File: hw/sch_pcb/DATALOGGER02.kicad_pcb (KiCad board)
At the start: 4 copper layers, 101.1 x 60.5 mm, 161 parts, among them IC1 CY15B108QN-40SXI, IC2 FM3164-G, IC3 LTC4041EUFD#PBF, J1 HEADER_2x01_PARALLEL, J10 HEADER_2x05_PARALLEL, J11 HEADER_2x07_PARALLEL, J12 HEADER_2x05_PARALLEL, J13 HEADER_2x02_PARALLEL, J14 Conn_01x06_Female, J2 HEADER_2x01, J23 MCX, J24 HEADER_2x03_PARALLEL, J3 HEADER_2x03, J4 HEADER_2x03_PARALLEL, J5 HEADER_2x03_PARALLEL, J6 MCC-SD (kouka z modulu), J7 Conn_01x06_Female, J8 Conn_01x07_Female, J9 Conn_01x04_Female, Q1 DMP2045UQ-7, Q2 DMTH3002LPS, Q3 DMTH3002LPS, U1 ISL21080CIH320Z-TK, U10 TPS631000DRLR, U11 SX1262, U12 PE4259, U2 LM4041CIM3-1.2(neosazovat), U3 ATMEGA1284P-AU, U4 TXS0108EPW, U5 ICM-20948, U6 TPS22965-Q1, U7 MS5611-01BA, U8 MIC5504-1.8YM5-TR, U9 TPS631000DRLR, Y2 6pF crystal - 32.768kHz, Y3 32MHz, Y6 8MHz LFXTAL083138

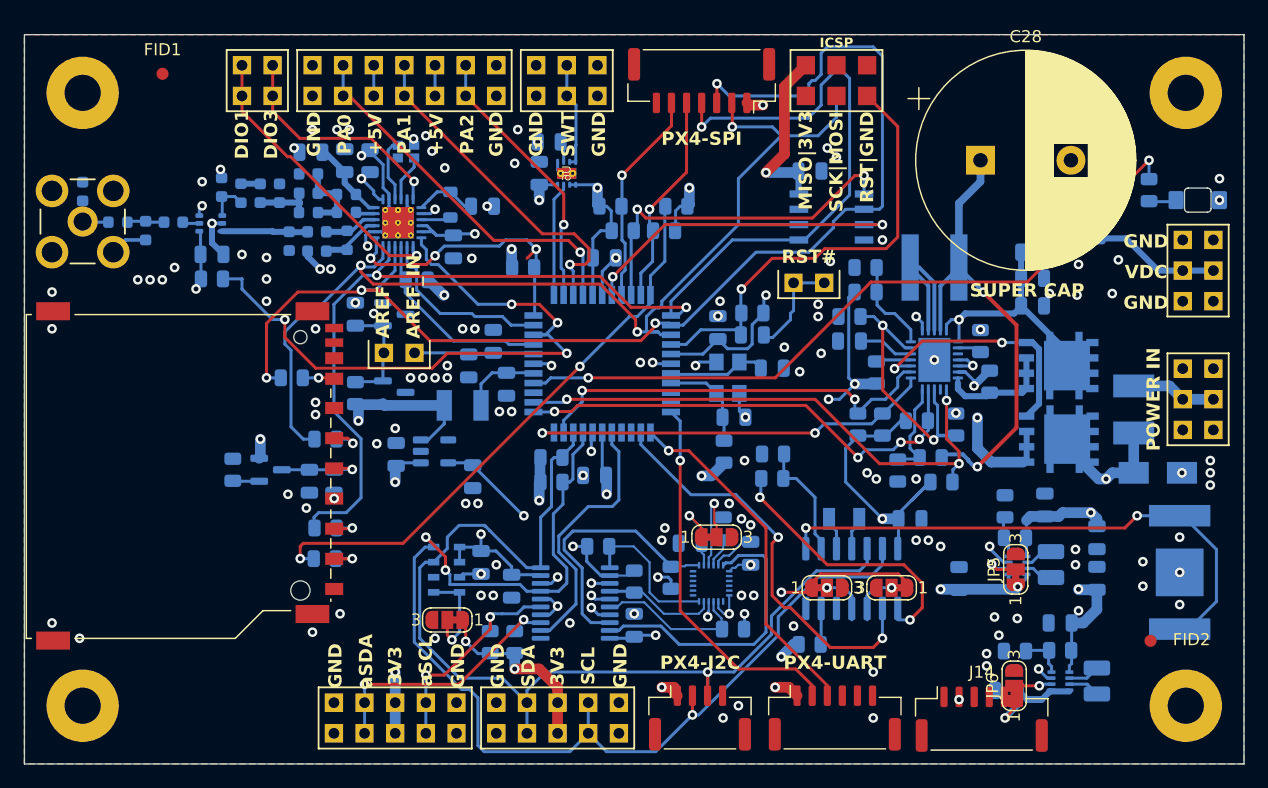
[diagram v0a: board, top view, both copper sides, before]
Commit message: úprava návrhu PCB
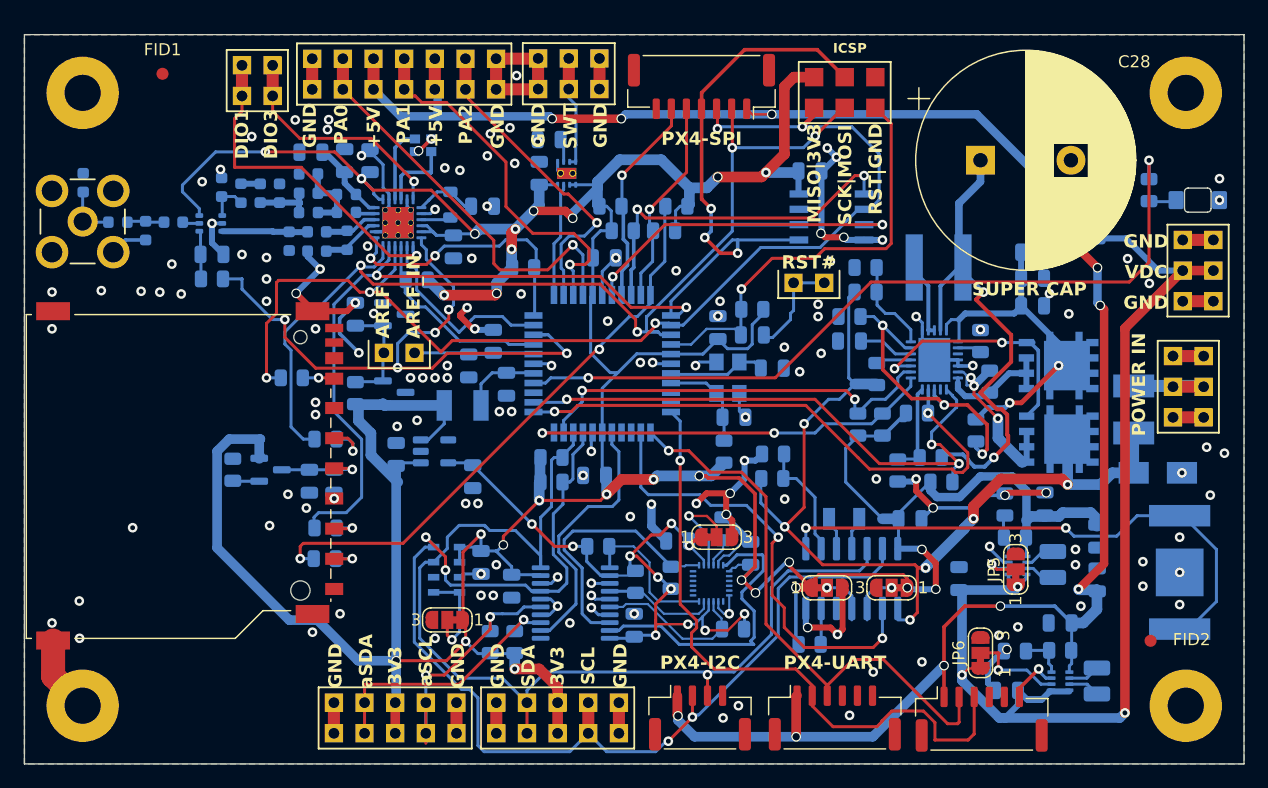
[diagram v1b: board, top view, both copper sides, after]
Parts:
- moved JP6 3.91 mm to (130.3, 127.7)
- moved R38 1.73 mm to (129.9, 109.3)
- moved Y3 1.51 mm to (84.1, 85.6)
- moved J24 1.32 mm to (147.5, 105.6)
- moved J3 1.20 mm to (119.0, 81.2)
- moved C15 1.05 mm to (105.2, 118.4)
- moved C59 0.74 mm to (55.9, 88.7)
- moved R32 0.63 mm to (125.0, 107.8)
- moved J4 0.59 mm to (96.2, 79.7)
- moved J11 0.54 mm to (82.5, 79.7)
- moved J8 0.49 mm to (107.2, 80.8)
- moved L2 0.34 mm to (126.8, 95.8)
- moved R3 0.31 mm to (111.4, 99.2)
- moved C21 0.19 mm to (94.5, 85.2)
- moved L4 0.16 mm to (136.3, 120.4)
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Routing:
- net GND: track 59.9 -> 191.8 mm, vias 138 -> 144
- net RX1: track 31.1 -> 53.4 mm
- net TX1: track 28.9 -> 46.6 mm
- net +3.3V: track 399.6 -> 390.0 mm, vias 25 -> 27
- net MISO_SPI: track 102.7 -> 94.8 mm, vias 4 -> 5
- net +1V8: track 64.0 -> 56.3 mm, vias 7 -> 11
- net SYSGD: track 39.1 -> 46.5 mm, vias 4 -> 2
- net Net-(IC3-SW_1): track 12.3 -> 6.30 mm
- net LED: track 60.2 -> 65.2 mm
- net Net-(JP6-C): track 3.15 -> 7.87 mm
- net /Power_management/Vdc: track 131.4 -> 127.5 mm
- net UNREG_POWER_INPUT: track 80.6 -> 77.1 mm, vias 5 -> 6
- net /Telemetry/DIO1: track 24.2 -> 27.8 mm
- net PA2: track 22.6 -> 26.1 mm
- net AUX_SDA_3V3: track 18.4 -> 21.8 mm
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- removed copper zone on In1.Cu, net +3.3V
- removed copper zone on In2.Cu, net GND
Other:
- copper layers 4 -> 2

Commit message: small changes in PCB layout
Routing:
- net GND: track 191.8 -> 180.6 mm, vias 144 -> 141
- net +3.3V: track 390.0 -> 384.2 mm
- net /Power_management/Vdc: track 127.5 -> 124.3 mm
- net SCK_SPI: track 90.5 -> 87.5 mm
- net /Telemetry/DIO1: track 27.8 -> 25.6 mm
- net Net-(IC3-SCAP): track 41.4 -> 39.8 mm
- net Net-(IC3-BSTFB): track 24.9 -> 23.5 mm
- net CNT2: track 36.4 -> 35.0 mm
- net BUSY_LORA: track 16.1 -> 14.9 mm
- net MISO_SPI: track 94.8 -> 93.6 mm
- net Net-(JP6-C): track 7.87 -> 6.96 mm
- net /Microcontroller/RST#: track 8.52 -> 7.88 mm
- net CAPFLT: track 48.0 -> 48.6 mm
- net +1V8: track 56.3 -> 56.1 mm, vias 11 -> 10
- net Net-(IC3-VIN): vias 3 -> 2

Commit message: Minor layout improvements.
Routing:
- net +3.3V: track 384.2 -> 383.5 mm
- net /Power_management/igate: track 21.2 -> 20.7 mm
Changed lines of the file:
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@@
 	)
 	(via
-		(at 75.184 106.934)
+		(at 74.4728 106.8324)
 		(size 0.8)
 		(drill 0.4)
@@
 	)
 	(via
-		(at 75.184 107.95)
+		(at 74.4982 108.1278)
 		(size 0.8)
 		(drill 0.4)
@@
 	)
 	(segment
-		(start 78.486 107.1245)
-		(end 80.7035 107.1245)
-		(width 0.889)
-		(layer "B.Cu")
-		(net "+3.3V")
-	)
-	(segment
 		(start 90.2 97.038)
 		(end 91.48 95.758)
@@
 	)
 	(segment
-		(start 79.7741 111.3121)
-		(end 79.7741 109.4921)
-		(width 0.889)
-		(layer "B.Cu")
-		(net "+3.3V")
-	)
-	(segment
 		(start 85.852 108.712)
 		(end 85.852 107.188)
@@
 	)
 	(segment
+		(start 79.7741 109.4921)
+		(end 78.74 108.458)
+		(width 0.889)
+		(layer "B.Cu")
+		(net "+3.3V")
+	)
+	(segment
 		(start 84.5185 110.0455)
 		(end 85.852 108.712)
@@
 	)
 	(segment
-		(start 91.75 92.575)
-		(end 88.781 92.575)
+		(start 80.664 112.202)
+		(end 79.7741 111.3121)
 		(width 0.889)
 		(layer "B.Cu")
@@
 	)
 	(segment
-		(start 136.794001 116.392999)
-		(end 135.636 116.392999)
+		(start 91.75 92.575)
+		(end 88.781 92.575)
 		(width 0.889)
 		(layer "B.Cu")
@@
 	)
 	(segment
-		(start 82 113.538)
-		(end 79.7741 111.3121)
+		(start 136.794001 116.392999)
+		(end 135.636 116.392999)
 		(width 0.889)
 		(layer "B.Cu")
@@
 	)
 	(segment
-		(start 78.74 107.3785)
-		(end 78.486 107.1245)
-		(width 0.889)
-		(layer "B.Cu")
-		(net "+3.3V")
-	)
-	(segment
 		(start 114.2 120.175)
 		(end 114.45 120.175)
@@
 	)
 	(segment
-		(start 79.7741 109.4921)
-		(end 78.74 108.458)
-		(width 0.889)
-		(layer "B.Cu")
-		(net "+3.3V")
-	)
-	(segment
 		(start 122.174 109.688)
 		(end 122.262 109.688)
@@
 	)
 	(segment
+		(start 79.7741 111.3121)
+		(end 79.7741 109.4921)
+		(width 0.889)
+		(layer "B.Cu")
+		(net "+3.3V")
+	)
+	(segment
+		(start 78.486 107.1245)
+		(end 80.7035 107.1245)
+		(width 0.889)
+		(layer "B.Cu")
+		(net "+3.3V")
+	)
+	(segment
 		(start 78.710214 128.35)
 		(end 75.344214 124.984)
@@
 	)
 	(segment
+		(start 78.74 108.458)
+		(end 78.74 107.3785)
+		(width 0.889)
+		(layer "B.Cu")
+		(net "+3.3V")
+	)
+	(segment
 		(start 90.13825 119.253)
 		(end 91.44 120.55475)
@@
 	)
 	(segment
+		(start 81.866 112.202)
+		(end 80.664 112.202)
+		(width 0.889)
+		(layer "B.Cu")
+		(net "+3.3V")
+	)
+	(segment
 		(start 123.5075 118.5545)
 		(end 123.444 118.618)
@@
 	)
 	(segment
-		(start 78.74 108.458)
-		(end 78.74 107.3785)
-		(width 0.889)
-		(layer "B.Cu")
-		(net "+3.3V")
-	)
-	(segment
 		(start 97.722 91.675)
 		(end 98.719 90.678)
@@
 	)
 	(segment
+		(start 80.7035 107.1245)
+		(end 80.772 107.056)
+		(width 0.889)
+		(layer "B.Cu")
+		(net "+3.3V")
+	)
+	(segment
 		(start 132.925 113.075)
 		(end 130.289798 113.075)
@@
 	)
 	(segment
-		(start 80.7035 107.1245)
-		(end 80.772 107.056)
+		(start 78.74 107.3785)
+		(end 78.486 107.1245)
 		(width 0.889)
 		(layer "B.Cu")
@@
 	)
 	(segment
+		(start 76.163 98.357698)
+		(end 76.163 108.749)
+		(width 0.25)
+		(layer "B.Cu")
+		(net "SCK_SPI")
+	)
+	(segment
 		(start 104.648 101.334)
 		(end 103.815 101.334)
@@
 	)
 	(segment
+		(start 76.163 108.749)
+		(end 75.097 109.815)
+		(width 0.25)
+		(layer "B.Cu")
+		(net "SCK_SPI")
+	)
+	(segment
 		(start 109.73 92.202)
 		(end 109.728 92.2)
@@
 	)
 	(segment
-		(start 76.163 108.916)
-		(end 75.097 109.982)
+		(start 80.772 94.996)
+		(end 80.772 93.98)
 		(width 0.25)
 		(layer "B.Cu")
@@
 	)
 	(segment
-		(start 80.772 94.996)
-		(end 80.772 93.98)
+		(start 79.068519 95.716347)
+		(end 78.936435 95.584263)
 		(width 0.25)
 		(layer "B.Cu")
@@
 	)
 	(segment
-		(start 79.068519 95.716347)
-		(end 78.936435 95.584263)
+		(start 75.097 109.815)
+		(end 75.097 109.982)
 		(width 0.25)
 		(layer "B.Cu")
@@
 	)
 	(segment
-		(start 76.163 98.357698)
-		(end 76.163 108.916)
-		(width 0.25)
-		(layer "B.Cu")
-		(net "SCK_SPI")
-	)
-	(segment
 		(start 78.936435 95.584263)
 		(end 76.163 98.357698)
@@
 	)
 	(segment
-		(start 129.155 104.702614)
-		(end 129.155 105.52)
-		(width 0.2)
+		(start 131.75 108.275)
+		(end 131.75 109.9)
+		(width 0.889)
 		(layer "B.Cu")
 		(net "Net-(IC3-VIN)")
 	)
 	(segment
-		(start 128.43 104.417)
-		(end 128.869386 104.417)
-		(width 0.2)
+		(start 131.75 109.9)
+		(end 132.467 110.617)
+		(width 0.889)
 		(layer "B.Cu")
 		(net "Net-(IC3-VIN)")
 	)
 	(segment
-		(start 131.75 109.9)
-		(end 133.737 111.887)
-		(width 0.889)
+		(start 129.155 104.702614)
+		(end 129.155 105.52)
+		(width 0.2)
 		(layer "B.Cu")
 		(net "Net-(IC3-VIN)")
 	)
 	(segment
-		(start 133.737 111.887)
-		(end 133.826 111.887)
-		(width 0.889)
+		(start 128.43 104.417)
+		(end 128.869386 104.417)
+		(width 0.2)
 		(layer "B.Cu")
 		(net "Net-(IC3-VIN)")
@@
 	)
 	(segment
+		(start 132.467 110.617)
+		(end 134.13 110.617)
+		(width 0.889)
+		(layer "B.Cu")
+		(net "Net-(IC3-VIN)")
+	)
+	(segment
 		(start 129.765585 105.572)
 		(end 129.765585 105.565415)
@@
 	)
 	(segment
-		(start 131.75 108.275)
-		(end 131.75 109.9)
-		(width 0.889)
-		(layer "B.Cu")
-		(net "Net-(IC3-VIN)")
-	)
-	(segment
 		(start 133.826 111.887)
 		(end 133.496 111.887)
@@
 	)
 	(segment
-		(start 134.109 101.981)
-		(end 134.62 101.981)
-		(width 0.5)
-		(layer "B.Cu")
-		(net "/Power_management/igate")
-	)
-	(segment
 		(start 120.396 101.854)
 		(end 122.174 101.854)
@@
 		(layer "B.Cu")
 		(hatch none 0.1)
-		(priority 30003)
+		(priority 30004)
 		(attr
 			(teardrop
@@
 		(layer "B.Cu")
 		(hatch none 0.1)
-		(priority 30004)
+		(priority 30005)
 		(attr
 			(teardrop
@@
 		(layer "B.Cu")
 		(hatch none 0.1)
-		(priority 30005)
+		(priority 30009)
 		(attr
 			(teardrop
@@
 		(layer "B.Cu")
 		(hatch none 0.1)
-		(priority 30007)
+		(priority 30003)
 		(attr
 			(teardrop
@@
 		(layer "B.Cu")
 		(hatch none 0.1)
-		(priority 30008)
+		(priority 30010)
 		(attr
 			(teardrop
@@
 		(layer "B.Cu")
 		(hatch none 0.1)
-		(priority 30009)
+		(priority 30007)
 		(attr
 			(teardrop
@@
 		(layer "B.Cu")
 		(hatch none 0.1)
-		(priority 30010)
+		(priority 30008)
 		(attr
 			(teardrop
